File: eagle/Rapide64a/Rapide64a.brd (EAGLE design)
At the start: 50 x 50 mm, 28 parts, among them IC1 MEGA64-A, J1 AVR_SPI_PRG_6PTH

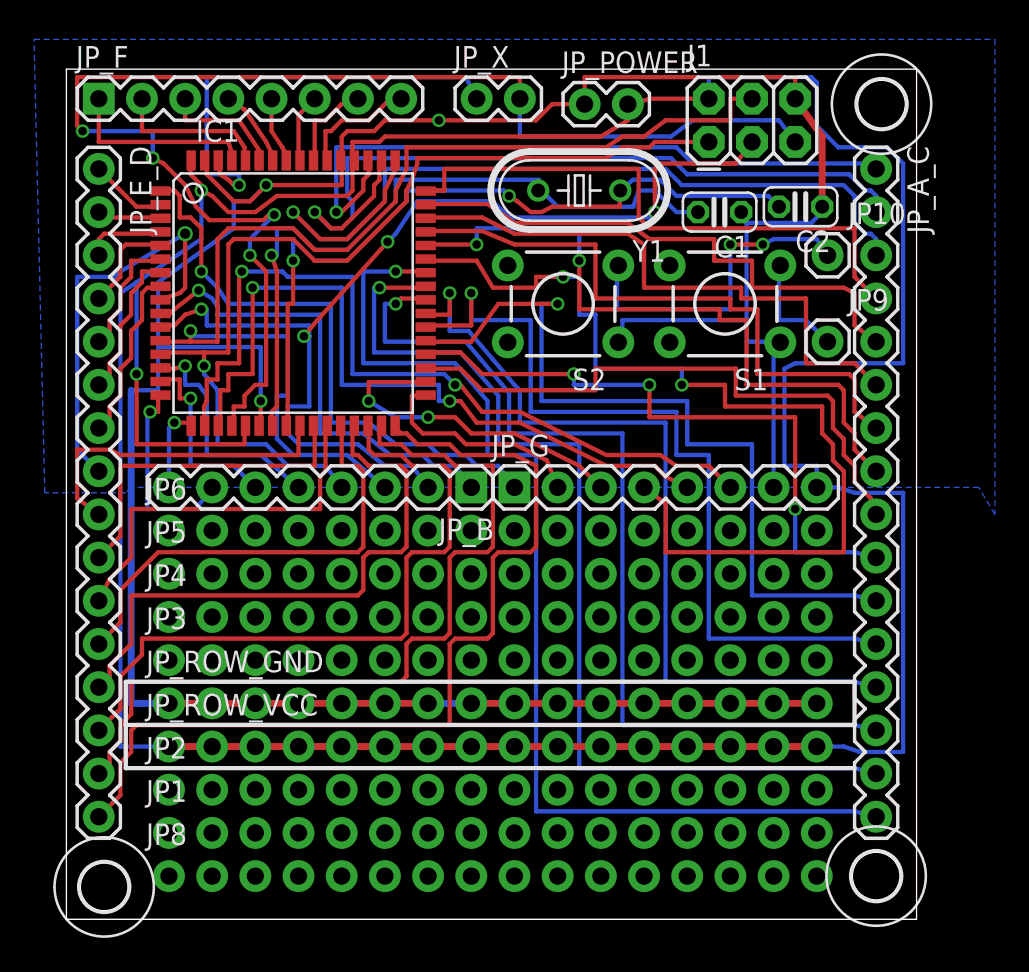
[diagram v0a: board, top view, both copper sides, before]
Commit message: v1.1 in progress : rewired with correct pins PE0 and PE1 for programming
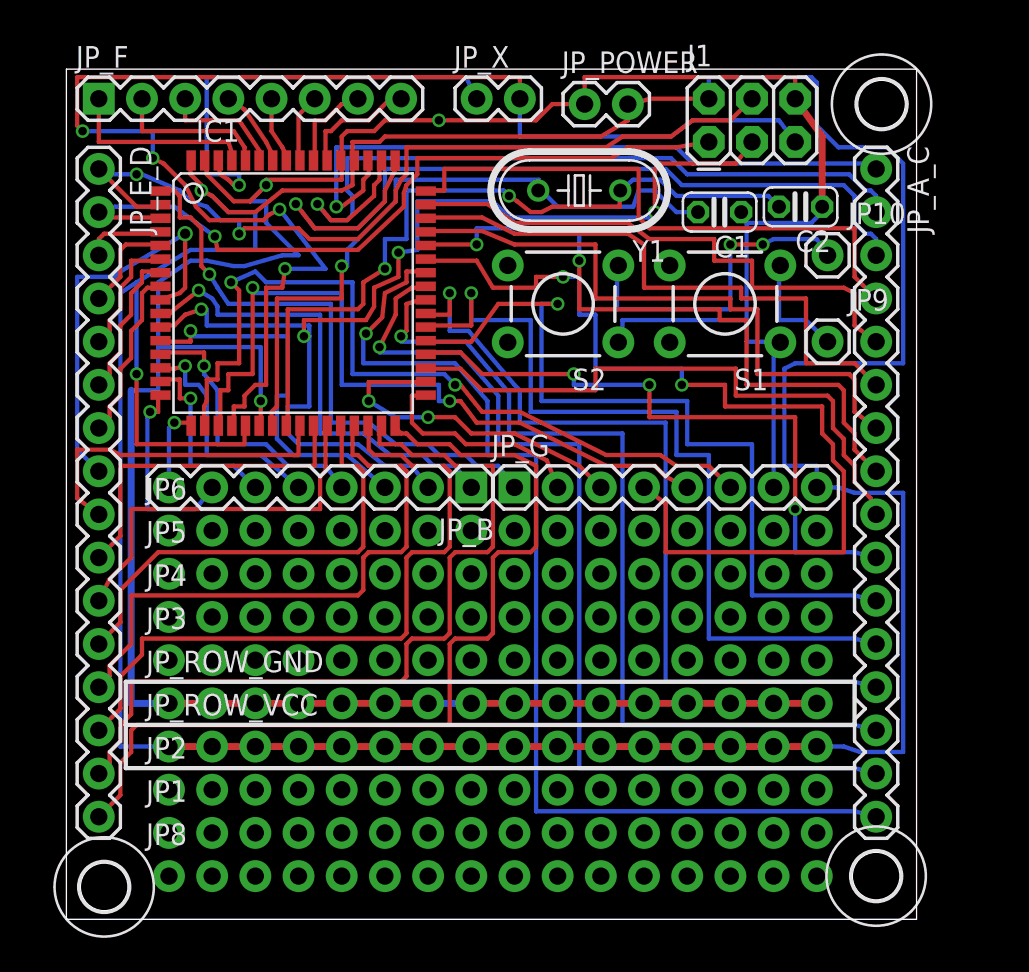
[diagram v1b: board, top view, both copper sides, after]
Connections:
- net N$15 renamed SCK
- net N$57 renamed RESET
- removed net N$1: IC1.2, JP_E_D.1
- removed net N$61: IC1.3, JP_E_D.2
- new net MISO: IC1.3, J1.1, JP_E_D.2
- new net MOSI: IC1.2, J1.4, JP_E_D.1
- net N$35: no longer J1.4
- net N$36: no longer J1.1
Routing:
- net MOSI: track 0.00 -> 49.6 mm, vias 0 -> 2
- net N$35: track 68.2 -> 22.7 mm
- net MISO: track 0.00 -> 44.7 mm, vias 0 -> 1
- net N$36: track 57.0 -> 16.5 mm
- net VCC: track 199.7 -> 205.4 mm
- net GND: track 168.3 -> 174.0 mm
- net N$1: track 4.41 -> 0.00 mm
- net RESET: track 79.7 -> 83.7 mm
- net N$61: track 3.94 -> 0.00 mm
- net SCK: track 61.6 -> 64.8 mm
- net N$51: track 54.6 -> 52.4 mm
- net N$59: track 41.9 -> 39.8 mm
- net N$50: track 59.3 -> 57.5 mm
- net N$49: track 64.2 -> 63.0 mm
- net N$17: track 50.7 -> 50.0 mm
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- removed copper zone on layer 16, net GND

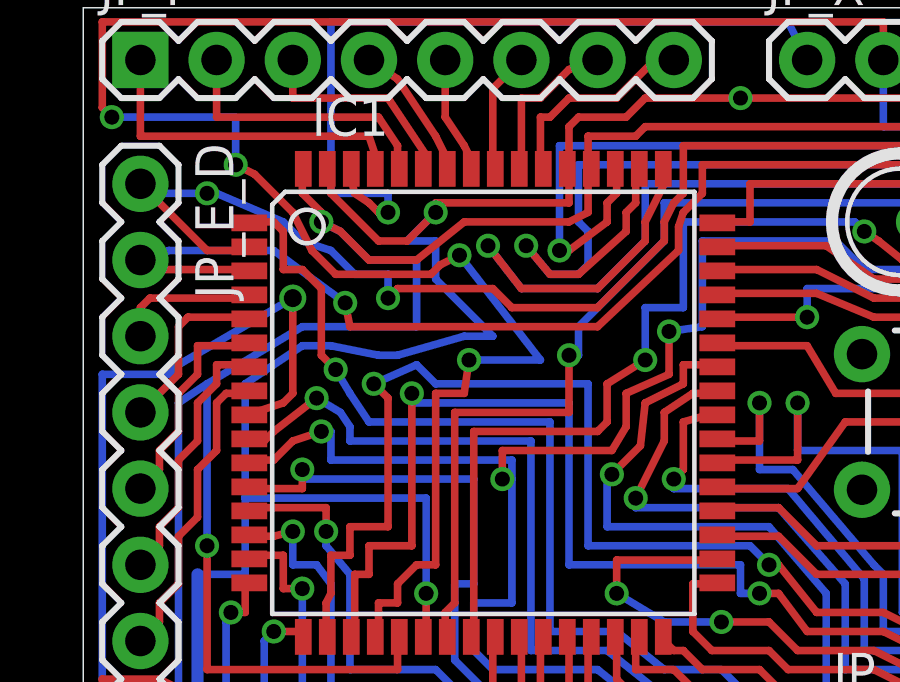
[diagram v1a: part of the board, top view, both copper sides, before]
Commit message: Continued v1.1, nicer wiring and changed label.
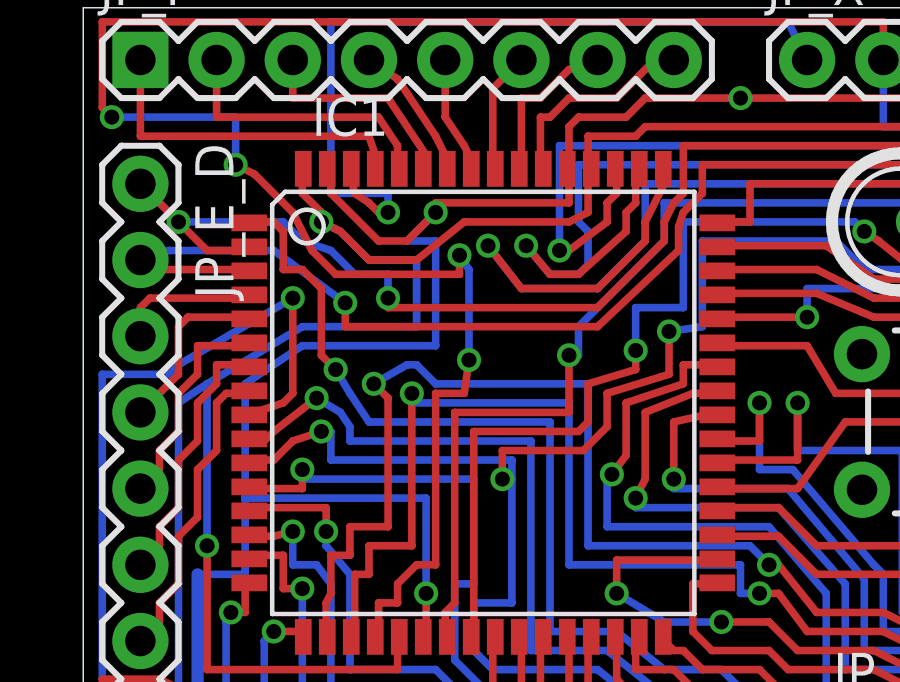
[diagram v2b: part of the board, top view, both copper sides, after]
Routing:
- net RESET: track 83.7 -> 81.0 mm
- net GND: track 174.0 -> 171.5 mm
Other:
- board text added: "Mar2013 v1.1"
- board text removed: "Dec2012 v1.0"
